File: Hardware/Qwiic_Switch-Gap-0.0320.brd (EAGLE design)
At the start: 30.5 x 20.3 mm, 47 parts, among them J7 ISP, U4 ATTINY84-ARDUINO

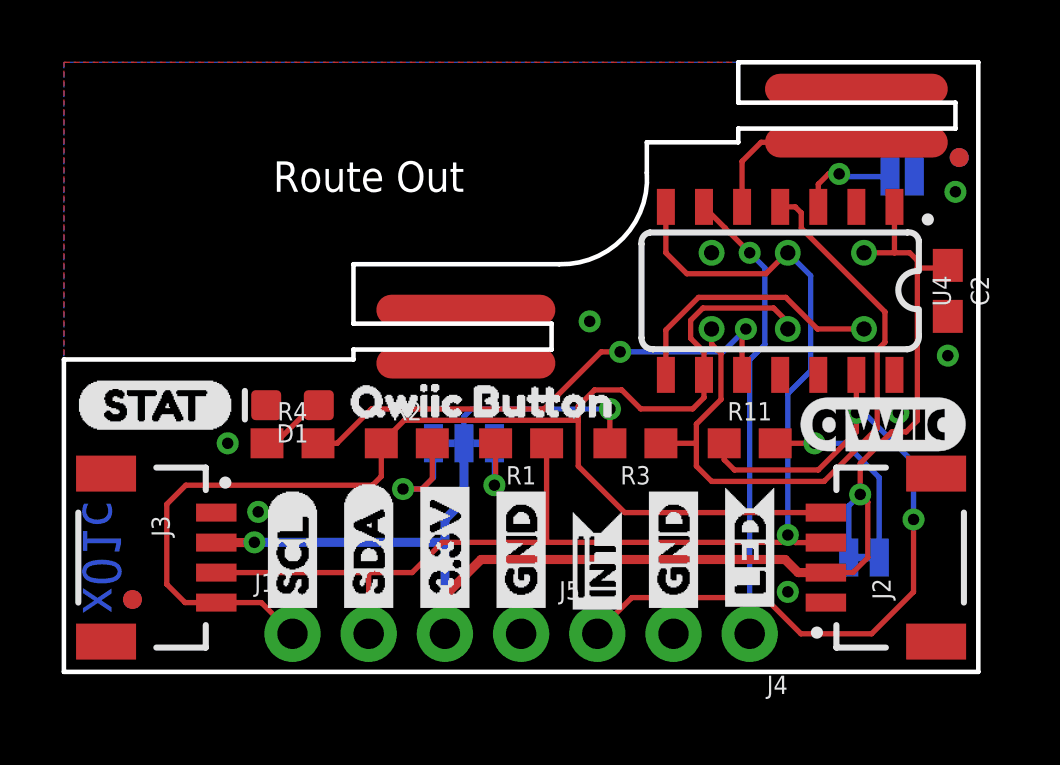
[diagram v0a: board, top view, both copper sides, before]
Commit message: Rename files with gap sizes.
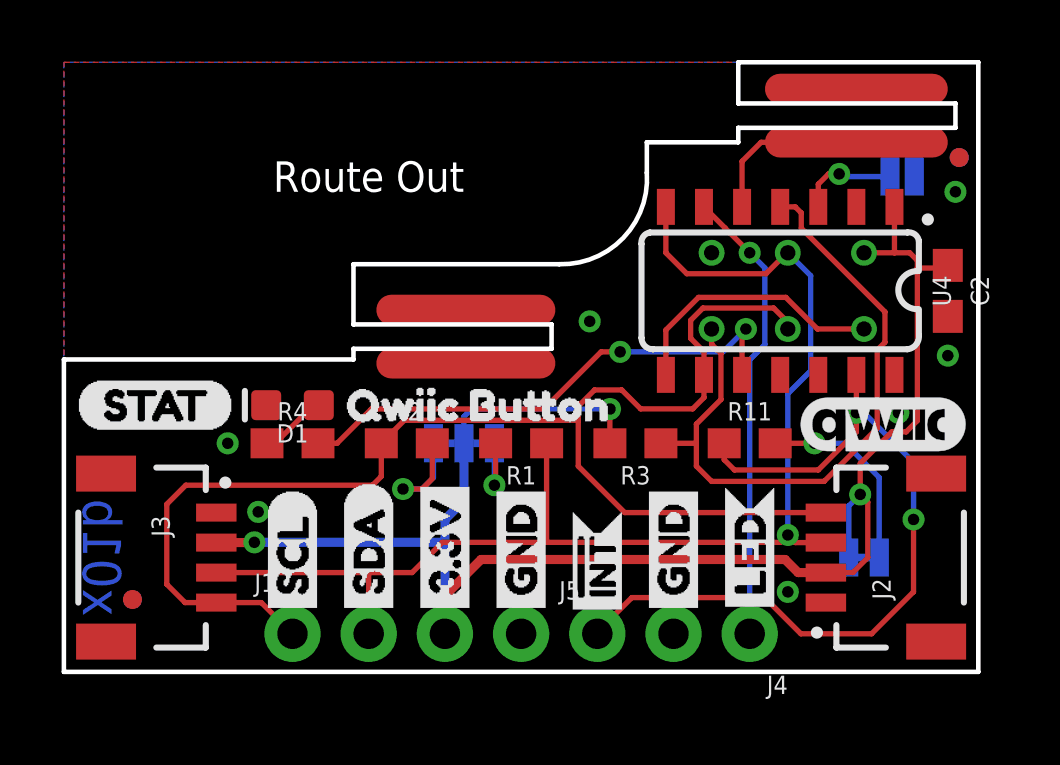
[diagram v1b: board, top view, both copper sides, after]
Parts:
- U$1, U$23: device buzzard_labels (4):QWIIC0 -> buzzard_labels (5):BUTTON1
- U$2, U$20: device buzzard_labels (4):BUTTON1 -> buzzard_labels (5):QWIIC0
- moved U$2 4.19 mm to (8.51, 8.89)
- moved U$1 3.94 mm to (12.6, 8.89)
- moved U$20 1.80 mm to (6.60, 8.26)
- moved U$23 1.31 mm to (6.99, 6.73)
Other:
- outline, holes or cut-outs redrawn
- board text added: "x01b"
- board text removed: "x01c"
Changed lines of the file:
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@@
 <?xml version="1.0" encoding="utf-8"?>
 <!DOCTYPE eagle SYSTEM "eagle.dtd">
-<eagle version="9.3.0">
+<eagle version="9.4.0">
 <drawing>
 <settings>
@@
 <layer number="23" name="tOrigins" color="15" fill="1" visible="yes" active="yes"/>
 <layer number="24" name="bOrigins" color="15" fill="1" visible="yes" active="yes"/>
-<layer number="25" name="tNames" color="7" fill="1" visible="yes" active="yes"/>
-<layer number="26" name="bNames" color="7" fill="1" visible="yes" active="yes"/>
-<layer number="27" name="tValues" color="7" fill="1" visible="yes" active="yes"/>
-<layer number="28" name="bValues" color="7" fill="1" visible="yes" active="yes"/>
-<layer number="29" name="tStop" color="7" fill="3" visible="yes" active="yes"/>
-<layer number="30" name="bStop" color="7" fill="6" visible="yes" active="yes"/>
-<layer number="31" name="tCream" color="7" fill="4" visible="yes" active="yes"/>
-<layer number="32" name="bCream" color="7" fill="5" visible="yes" active="yes"/>
-<layer number="33" name="tFinish" color="6" fill="3" visible="yes" active="yes"/>
-<layer number="34" name="bFinish" color="6" fill="6" visible="yes" active="yes"/>
-<layer number="35" name="tGlue" color="7" fill="4" visible="yes" active="yes"/>
-<layer number="36" name="bGlue" color="7" fill="5" visible="yes" active="yes"/>
-<layer number="37" name="tTest" color="7" fill="1" visible="yes" active="yes"/>
-<layer number="38" name="bTest" color="7" fill="1" visible="yes" active="yes"/>
-<layer number="39" name="tKeepout" color="4" fill="11" visible="yes" active="yes"/>
-<layer number="40" name="bKeepout" color="1" fill="11" visible="yes" active="yes"/>
-<layer number="41" name="tRestrict" color="4" fill="10" visible="yes" active="yes"/>
-<layer number="42" name="bRestrict" color="1" fill="10" visible="yes" active="yes"/>
-<layer number="43" name="vRestrict" color="2" fill="10" visible="yes" active="yes"/>
-<layer number="44" name="Drills" color="7" fill="1" visible="yes" active="yes"/>
+<layer number="25" name="tNames" color="7" fill="1" visible="no" active="yes"/>
+<layer number="26" name="bNames" color="7" fill="1" visible="no" active="yes"/>
+<layer number="27" name="tValues" color="7" fill="1" visible="no" active="yes"/>
+<layer number="28" name="bValues" color="7" fill="1" visible="no" active="yes"/>
+<layer number="29" name="tStop" color="7" fill="3" visible="no" active="yes"/>
+<layer number="30" name="bStop" color="7" fill="6" visible="no" active="yes"/>
+<layer number="31" name="tCream" color="7" fill="4" visible="no" active="yes"/>
+<layer number="32" name="bCream" color="7" fill="5" visible="no" active="yes"/>
+<layer number="33" name="tFinish" color="6" fill="3" visible="no" active="yes"/>
+<layer number="34" name="bFinish" color="6" fill="6" visible="no" active="yes"/>
+<layer number="35" name="tGlue" color="7" fill="4" visible="no" active="yes"/>
+<layer number="36" name="bGlue" color="7" fill="5" visible="no" active="yes"/>
+<layer number="37" name="tTest" color="7" fill="1" visible="no" active="yes"/>
+<layer number="38" name="bTest" color="7" fill="1" visible="no" active="yes"/>
+<layer number="39" name="tKeepout" color="4" fill="11" visible="no" active="yes"/>
+<layer number="40" name="bKeepout" color="1" fill="11" visible="no" active="yes"/>
+<layer number="41" name="tRestrict" color="4" fill="10" visible="no" active="yes"/>
+<layer number="42" name="bRestrict" color="1" fill="10" visible="no" active="yes"/>
+<layer number="43" name="vRestrict" color="2" fill="10" visible="no" active="yes"/>
+<layer number="44" name="Drills" color="7" fill="1" visible="no" active="yes"/>
 <layer number="45" name="Holes" color="7" fill="1" visible="yes" active="yes"/>
-<layer number="46" name="Milling" color="3" fill="1" visible="yes" active="yes"/>
-<layer number="47" name="Measures" color="7" fill="1" visible="yes" active="yes"/>
-<layer number="48" name="Document" color="7" fill="1" visible="yes" active="yes"/>
-<layer number="49" name="Reference" color="7" fill="1" visible="yes" active="yes"/>
-<layer number="50" name="dxf" color="7" fill="1" visible="yes" active="yes"/>
+<layer number="46" name="Milling" color="3" fill="1" visible="no" active="yes"/>
+<layer number="47" name="Measures" color="7" fill="1" visible="no" active="yes"/>
+<layer number="48" name="Document" color="7" fill="1" visible="no" active="yes"/>
+<layer number="49" name="Reference" color="7" fill="1" visible="no" active="yes"/>
+<layer number="50" name="dxf" color="7" fill="1" visible="no" active="yes"/>
 <layer number="51" name="tDocu" color="6" fill="1" visible="yes" active="yes"/>
-<layer number="52" name="bDocu" color="7" fill="1" visible="yes" active="yes"/>
+<layer number="52" name="bDocu" color="7" fill="1" visible="no" active="yes"/>
 <layer number="91" name="Nets" color="2" fill="1" visible="no" active="no"/>
 <layer number="92" name="Busses" color="1" fill="1" visible="no" active="no"/>
@@
 <wire x1="30.48" y1="0" x2="30.48" y2="20.32" width="0.1524" layer="20"/>
 <wire x1="30.48" y1="20.32" x2="22.479" y2="20.32" width="0.1524" layer="20"/>
-<wire x1="22.479" y1="20.32" x2="22.479" y2="18.9738" width="0.1524" layer="20"/>
-<wire x1="22.479" y1="18.9738" x2="29.718" y2="18.9738" width="0.1524" layer="20"/>
-<wire x1="29.718" y1="18.9738" x2="29.718" y2="18.1102" width="0.1524" layer="20"/>
-<wire x1="29.718" y1="18.1102" x2="22.479" y2="18.1102" width="0.1524" layer="20"/>
-<wire x1="22.479" y1="18.1102" x2="22.479" y2="17.653" width="0.1524" layer="20"/>
+<wire x1="22.479" y1="20.32" x2="22.479" y2="18.9484" width="0.1524" layer="20"/>
+<wire x1="22.479" y1="18.9484" x2="29.718" y2="18.9484" width="0.1524" layer="20"/>
+<wire x1="29.718" y1="18.9484" x2="29.718" y2="18.1356" width="0.1524" layer="20"/>
+<wire x1="29.718" y1="18.1356" x2="22.479" y2="18.1356" width="0.1524" layer="20"/>
+<wire x1="22.479" y1="18.1356" x2="22.479" y2="17.653" width="0.1524" layer="20"/>
 <wire x1="22.479" y1="17.653" x2="19.431" y2="17.653" width="0.1524" layer="20"/>
 <wire x1="16.51" y1="13.589" x2="9.652" y2="13.589" width="0.1524" layer="20"/>
-<wire x1="9.652" y1="13.589" x2="9.652" y2="11.6078" width="0.1524" layer="20"/>
-<wire x1="9.652" y1="11.6078" x2="16.256" y2="11.6078" width="0.1524" layer="20"/>
-<wire x1="16.256" y1="11.6078" x2="16.256" y2="10.7442" width="0.1524" layer="20"/>
-<wire x1="16.256" y1="10.7442" x2="9.652" y2="10.7442" width="0.1524" layer="20"/>
-<wire x1="9.652" y1="10.7442" x2="9.652" y2="10.414" width="0.1524" layer="20"/>
+<wire x1="9.652" y1="13.589" x2="9.652" y2="11.5824" width="0.1524" layer="20"/>
+<wire x1="9.652" y1="11.5824" x2="16.256" y2="11.5824" width="0.1524" layer="20"/>
+<wire x1="16.256" y1="11.5824" x2="16.256" y2="10.7696" width="0.1524" layer="20"/>
+<wire x1="16.256" y1="10.7696" x2="9.652" y2="10.7696" width="0.1524" layer="20"/>
+<wire x1="9.652" y1="10.7696" x2="9.652" y2="10.414" width="0.1524" layer="20"/>
 <wire x1="9.652" y1="10.414" x2="0" y2="10.414" width="0.1524" layer="20"/>
 <wire x1="0" y1="10.414" x2="0" y2="0" width="0.1524" layer="20"/>
-<text x="1.27" y="3.81" size="1.27" layer="16" font="vector" ratio="15" rot="SMR90" align="center">x01c</text>
+<text x="1.27" y="3.81" size="1.27" layer="16" font="vector" ratio="15" rot="SMR90" align="center">x01b</text>
 <wire x1="23.876" y1="17.653" x2="28.956" y2="17.653" width="1.016" layer="29"/>
 <wire x1="23.876" y1="19.431" x2="28.956" y2="19.431" width="1.016" layer="29"/>
@@
 <element name="U$19" library="buzzard_labels (3)" package="LED2" value="" x="22.86" y="1.651" smashed="yes" rot="MR90"/>
 <element name="U$21" library="buzzard_labels (3)" package="STAT1" value="" x="0.381" y="8.89" smashed="yes"/>
-<element name="U$1" library="buzzard_labels (4)" package="QWIIC0" value="" x="8.636" y="9.017" smashed="yes"/>
-<element name="U$2" library="buzzard_labels (4)" package="BUTTON1" value="" x="12.7" y="9.017" smashed="yes"/>
-<element name="U$20" library="buzzard_labels (4)" package="BUTTON1" value="" x="6.858" y="6.477" smashed="yes" rot="MR0"/>
-<element name="U$23" library="buzzard_labels (4)" package="QWIIC0" value="" x="6.35" y="7.874" smashed="yes" rot="MR0"/>
+<element name="U$1" library="buzzard_labels (5)" package="BUTTON1" value="" x="12.573" y="8.89" smashed="yes"/>
+<element name="U$2" library="buzzard_labels (5)" package="QWIIC0" value="" x="8.509" y="8.89" smashed="yes"/>
+<element name="U$20" library="buzzard_labels (5)" package="QWIIC0" value="" x="6.604" y="8.255" smashed="yes" rot="MR0"/>
+<element name="U$23" library="buzzard_labels (5)" package="BUTTON1" value="" x="6.985" y="6.731" smashed="yes" rot="MR0"/>
 <element name="U$24" library="SparkFun-Aesthetics" package="QWIIC_5.5MM" value="" x="27.305" y="8.255" smashed="yes"/>
 </elements>
